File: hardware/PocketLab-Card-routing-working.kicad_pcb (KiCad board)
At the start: 4 copper layers, 85.6 x 54 mm, 260 parts, among them J1 USB-C DATA/POWER, J2 microSD, J3 EXTERNAL 400uH LF COIL, J4 PROTECTED 1S LiPo 3.7V, J5 30-PIN 2.54mm DUPONT GRID, Q1 AO3400A IR DRIVER, Q2 CSD16406Q3 DISCHARGE, Q3 CSD16406Q3 CHARGE, SW1 RESET, SW2 BOOT, SW3 UP, SW4 DOWN, SW5 MAIN POWER OFF / ON, SW6 PAIR, SW7 SELECT, SW8 AUX CONFIG, U1 ESP32-S3-WROOM-1-N8R2, U10 BMI270 (FULL OPTION), U11 BMP390 (FULL OPTION), U12 PCF8563T, U13 TSOP75338WTR 38kHz, U14 BQ29700DSE, U15 TPS2553DBVR 500mA LIMIT, U16 USBLC6-4SC6Y, U17 TPS22919DCKR LF 5V LOAD SWITCH, U18 TCA9534PWR INTERNAL CONTROL, U19 SRV05-4MR6T1G SD ESD, U2 PN5321A3HN/C106, U20 SN74AHCT1G126DBVR RGB LEVEL S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, U21 SN74LV125ATPWR LF/SPI 3V3-TO-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, U22 SN74LVC1G126DBVR LF 5V-TO-3V3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, U23 ATECC608C-SSHDA-T, U24 SRV05-4MR6T1G J5 BUS ESD, U25 SRV05-4MR6T1G J5 SPI ESD, U3 E07-900MM10S 855-925MHz, U4 HTRC11001T/03EE,11 125kHz, U5 BQ24074RGTR, U6 TPS63070RNMR 3V3, U7 TPS61023DRLR 5V BOOST, U8 MAX17048G+T10, U9 TCA9535PWR, Y301 27.12MHz crystal (pins 2/4 sh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, Y501 4MHz 5V CMOS OSCILLATOR, Y701 32.768kHz CL=7pF

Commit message: Route additional drill-clearance offenders
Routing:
- net /VBUS_FUSED: track 65.0 -> 71.1 mm
- net /+3V3: track 392.0 -> 395.6 mm
- net /PWR_SW_ON: track 36.8 -> 38.6 mm
- net /NFC_RX: track 38.9 -> 40.5 mm
- net /CHARGER_CHG_N: track 36.4 -> 37.6 mm
- net /JTAG_STRAP_TP: track 26.9 -> 27.9 mm
- net /SUBGHZ_CS_N: track 23.1 -> 23.8 mm
- net /RGB_BUF_5V: track 27.6 -> 28.4 mm

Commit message: Reduce NFC and SD drill conflicts
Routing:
- net /NFC_TX2_F: track 44.8 -> 47.7 mm
- net /SD_MISO: track 84.2 -> 87.0 mm
- net /BQ_EN1: track 58.1 -> 59.9 mm
- net /NFC_LOOP_B: track 41.6 -> 43.1 mm
- net /NFC_IRQ_N: track 17.8 -> 19.1 mm

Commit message: Reroute auxiliary and expansion signals
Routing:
- net /EX1: track 45.6 -> 48.0 mm
- net /PAIR_N: track 61.5 -> 63.3 mm
- net /AUX5_EN: track 33.7 -> 35.4 mm
- net /RGB_DIN1: track 45.6 -> 47.0 mm

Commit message: Reduce GPIO and low frequency drill conflicts
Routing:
- net /AUX5_FAULT_N: track 76.9 -> 80.2 mm
- net /GPIO8_MCU: track 109.6 -> 110.9 mm
- net /IR_LED_A1: track 50.3 -> 51.5 mm
- net /LF_DIN_5V: track 51.4 -> 52.5 mm
- net /LF_RFID_EN: track 51.3 -> 51.9 mm

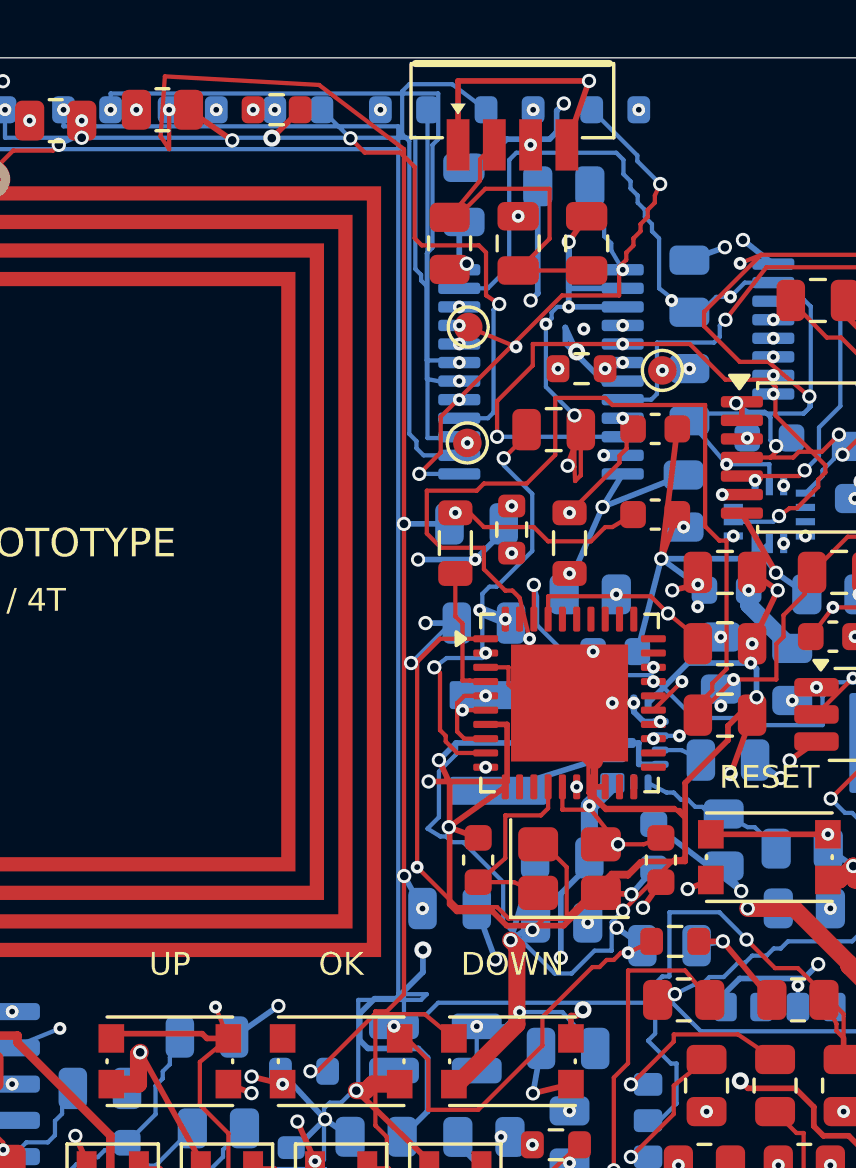
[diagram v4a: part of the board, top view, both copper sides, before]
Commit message: Reroute GPIO and NFC drill offenders
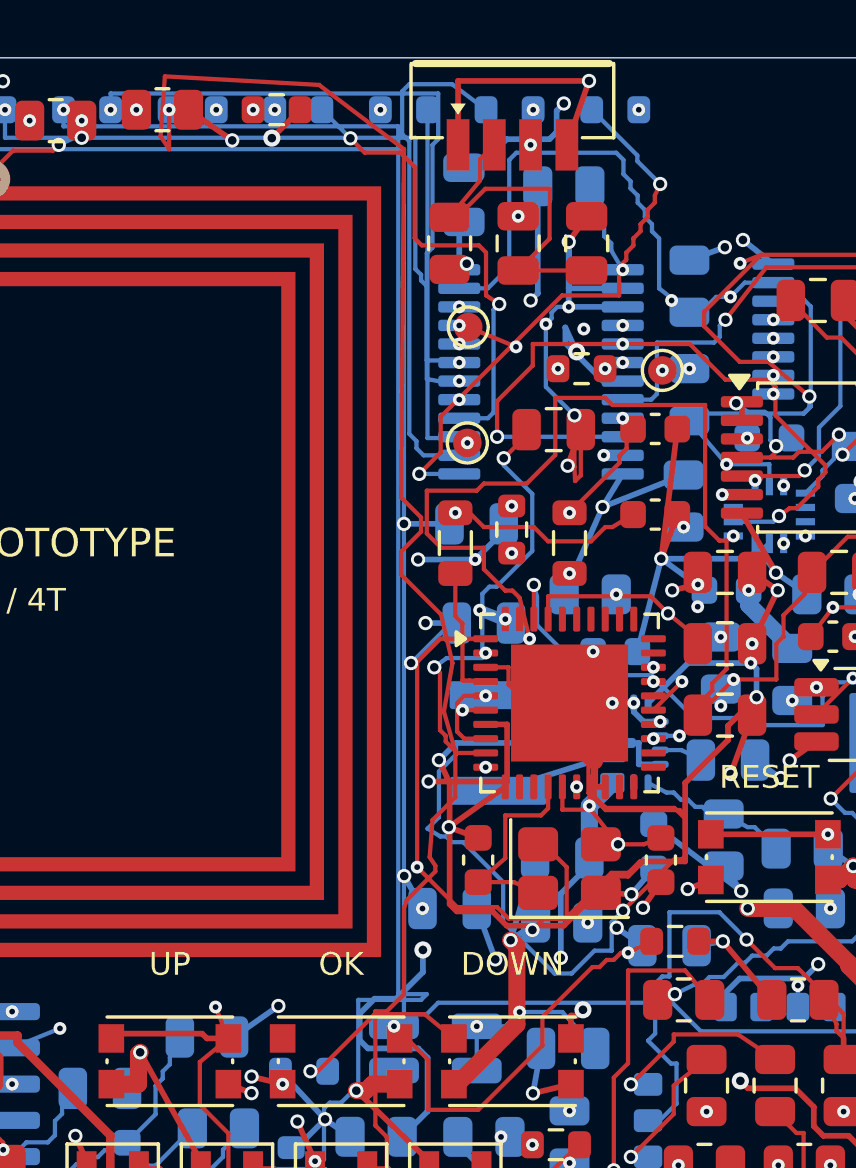
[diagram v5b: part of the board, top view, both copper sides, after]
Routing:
- net /EX4: track 70.0 -> 72.2 mm
- net /GPIO43_MCU: track 68.3 -> 69.9 mm
- net /GPIO48: track 38.8 -> 40.1 mm
- net /NFC_RESET_N: track 63.7 -> 64.5 mm

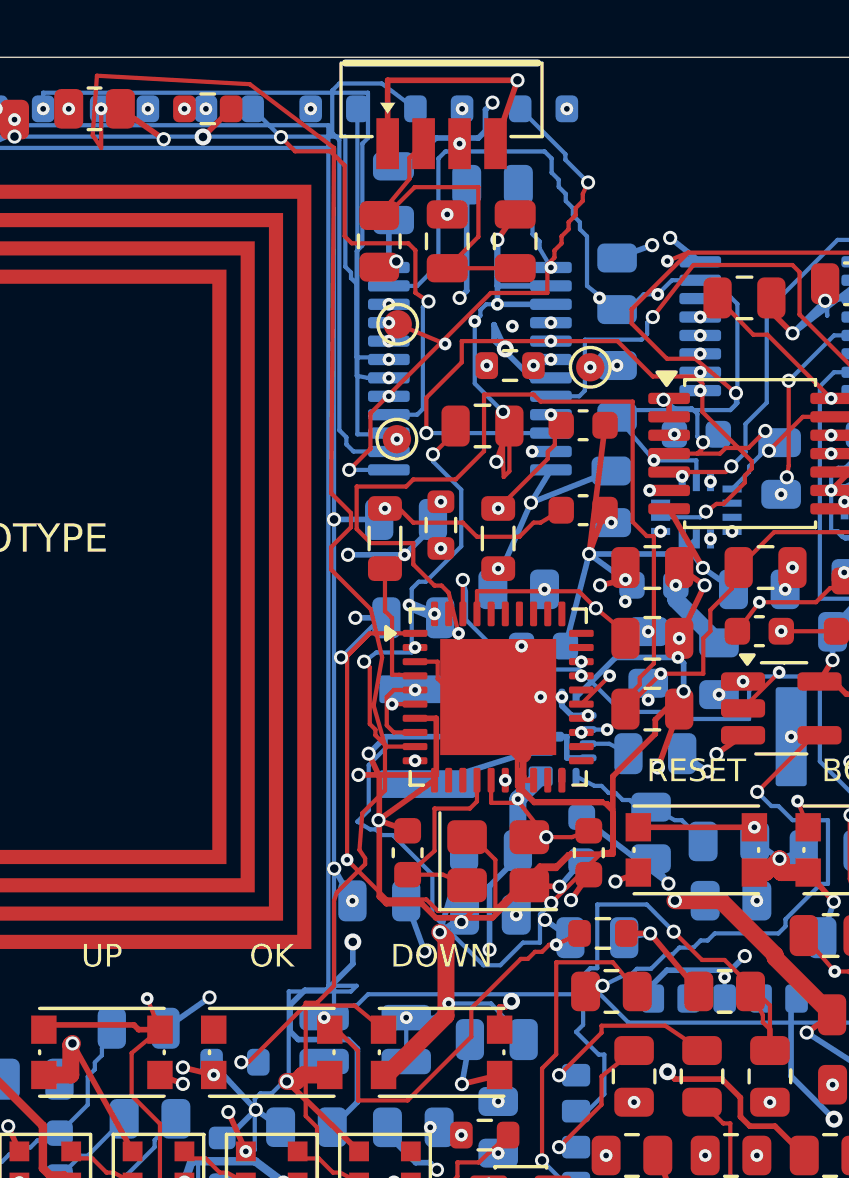
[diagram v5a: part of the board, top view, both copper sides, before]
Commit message: Reduce sensor and low frequency drill conflicts
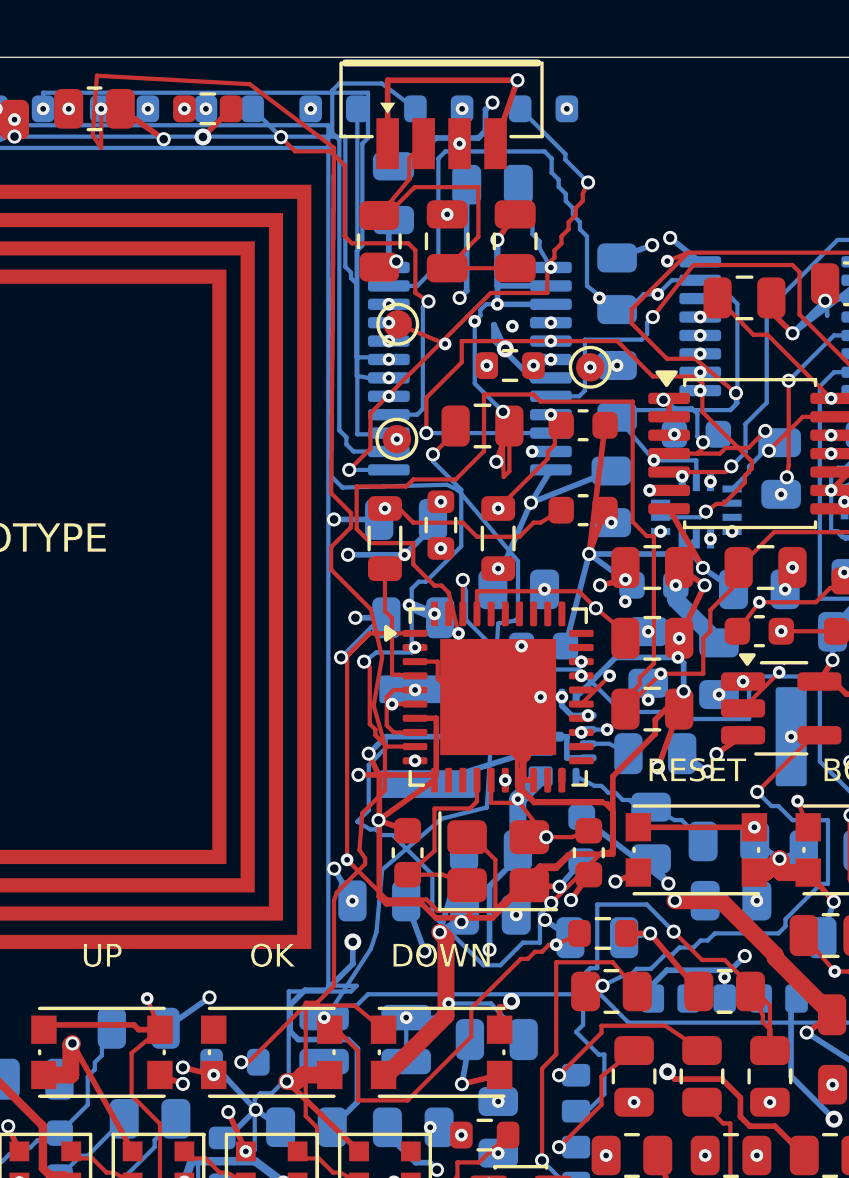
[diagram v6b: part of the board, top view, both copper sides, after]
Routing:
- net /BOARD_TEMP_ADC: track 122.3 -> 130.5 mm
- net /GPIO38_MCU: track 38.4 -> 39.9 mm
- net /LF_RFID_EN: track 51.9 -> 53.0 mm
- net /LF_5V: track 71.5 -> 72.1 mm
